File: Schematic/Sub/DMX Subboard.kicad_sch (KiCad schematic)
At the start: 6 parts, among them J1 OLED, J2 Connector, SW1 Back, SW2 Up, SW3 Down, SW4 Confirm

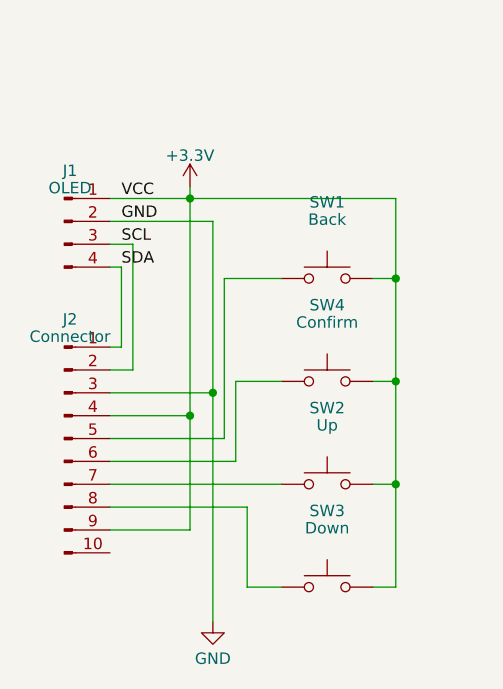
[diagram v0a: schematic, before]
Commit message: First OLED support
- SSD1306 support added
- OLED menu added (wip)
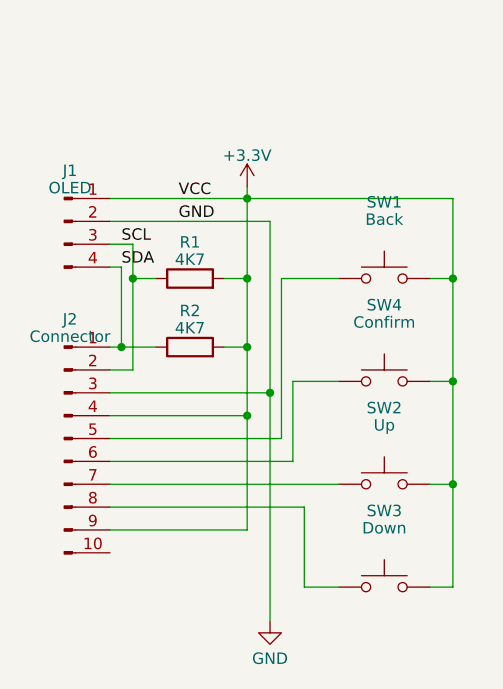
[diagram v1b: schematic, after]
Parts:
- added R1, R2: 4K7, Resistor_SMD:R_0603_1608Metric_Pad0.98x0.95mm_HandSolder, symbol Device:R
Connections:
- net +3.3V: now also R1.2, R2.2
- net SCL: now also R1.1
- net SDA: now also R2.1
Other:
- moved on the sheet: SW1, SW2, SW3, SW4

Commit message: Added support for different OLED-pinning
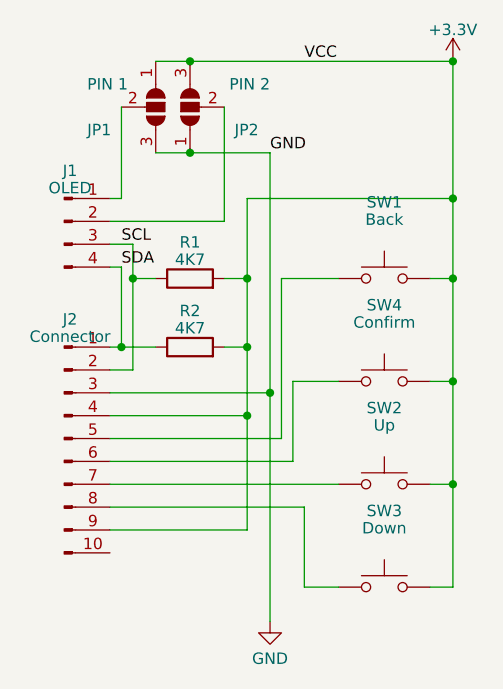
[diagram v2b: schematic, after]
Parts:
- added JP1: PIN 1, Jumper:SolderJumper-3_P2.0mm_Open_TrianglePad1.0x1.5mm, symbol Jumper:SolderJumper_3_Open
- added JP2: PIN 2, Jumper:SolderJumper-3_P2.0mm_Open_TrianglePad1.0x1.5mm, symbol Jumper:SolderJumper_3_Open
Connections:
- net +3.3V: now also JP1.1 (A), JP2.3 (B); no longer J1.1 (Pin_1)
- net GND: now also JP1.3 (B), JP2.1 (A); no longer J1.2 (Pin_2)
- new net: J1.2 (Pin_2), JP2.2 (C)
- new net: J1.1 (Pin_1), JP1.2 (C)
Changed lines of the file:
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@@
   (junction (at 69.85 54.61) (diameter 0) (color 0 0 0 0)
   )
-  (junction (at 46.99 34.29) (diameter 0) (color 0 0 0 0)
+  (junction (at 40.64 29.21) (diameter 0) (color 0 0 0 0)
+  )
+  (junction (at 40.64 19.05) (diameter 0) (color 0 0 0 0)
   )
   (junction (at 34.29 43.18) (diameter 0) (color 0 0 0 0)
@@
   (junction (at 69.85 66.04) (diameter 0) (color 0 0 0 0)
   )
+  (junction (at 69.85 19.05) (diameter 0) (color 0 0 0 0)
+  )
   (junction (at 46.99 43.18) (diameter 0) (color 0 0 0 0)
   )
+  (junction (at 69.85 34.29) (diameter 0) (color 0 0 0 0)
+  )
   (wire (pts (xy 31.75 63.5) (xy 52.07 63.5))
     (stroke (width 0) (type default))
   )
-  (wire (pts (xy 31.75 36.83) (xy 49.53 36.83))
-    (stroke (width 0) (type default))
-  )
-  (wire (pts (xy 49.53 36.83) (xy 49.53 55.88))
+  (wire (pts (xy 44.45 24.13) (xy 44.45 36.83))
+    (stroke (width 0) (type default))
+  )
+  (wire (pts (xy 49.53 29.21) (xy 49.53 55.88))
     (stroke (width 0) (type default))
   )
@@
     (stroke (width 0) (type default))
   )
-  (wire (pts (xy 31.75 34.29) (xy 46.99 34.29))
+  (wire (pts (xy 40.64 29.21) (xy 49.53 29.21))
+    (stroke (width 0) (type default))
+  )
+  (wire (pts (xy 44.45 36.83) (xy 31.75 36.83))
     (stroke (width 0) (type default))
   )
@@
     (stroke (width 0) (type default))
   )
+  (wire (pts (xy 33.02 34.29) (xy 31.75 34.29))
+    (stroke (width 0) (type default))
+  )
+  (wire (pts (xy 46.99 34.29) (xy 69.85 34.29))
+    (stroke (width 0) (type default))
+  )
   (wire (pts (xy 31.75 68.58) (xy 53.34 68.58))
     (stroke (width 0) (type default))
@@
     (stroke (width 0) (type default))
   )
-  (wire (pts (xy 46.99 33.02) (xy 46.99 34.29))
-    (stroke (width 0) (type default))
-  )
   (wire (pts (xy 34.29 53.34) (xy 34.29 43.18))
     (stroke (width 0) (type default))
@@
     (stroke (width 0) (type default))
   )
+  (wire (pts (xy 69.85 19.05) (xy 69.85 34.29))
+    (stroke (width 0) (type default))
+  )
   (wire (pts (xy 69.85 54.61) (xy 69.85 66.04))
     (stroke (width 0) (type default))
   )
-  (wire (pts (xy 69.85 34.29) (xy 46.99 34.29))
+  (wire (pts (xy 33.02 24.13) (xy 33.02 34.29))
     (stroke (width 0) (type default))
   )
@@
   )
   (wire (pts (xy 33.02 50.8) (xy 36.83 50.8))
+    (stroke (width 0) (type default))
+  )
+  (wire (pts (xy 36.83 29.21) (xy 40.64 29.21))
+    (stroke (width 0) (type default))
+  )
+  (wire (pts (xy 40.64 19.05) (xy 69.85 19.05))
+    (stroke (width 0) (type default))
+  )
+  (wire (pts (xy 36.83 19.05) (xy 40.64 19.05))
     (stroke (width 0) (type default))
   )
@@
     (effects (font (size 1.27 1.27)) (justify left bottom))
   )
-  (label "GND" (at 39.37 36.83 0) (fields_autoplaced)
+  (label "GND" (at 49.53 29.21 0) (fields_autoplaced)
     (effects (font (size 1.27 1.27)) (justify left bottom))
   )
@@
     (effects (font (size 1.27 1.27)) (justify left bottom))
   )
-  (label "VCC" (at 39.37 34.29 0) (fields_autoplaced)
+  (label "VCC" (at 53.34 19.05 0) (fields_autoplaced)
     (effects (font (size 1.27 1.27)) (justify left bottom))
   )
@@
     )
   )
+  (symbol (lib_id "Jumper:SolderJumper_3_Open") (at 40.64 24.13 90) (unit 1)
+    (in_bom yes) (on_board yes) (dnp no)
+    (property "Reference" "JP2" (at 48.26 26.67 90)
+      (effects (font (size 1.27 1.27)) (justify left))
+    )
+    (property "Value" "PIN 2" (at 49.53 21.59 90)
+      (effects (font (size 1.27 1.27)) (justify left))
+    )
+    (property "Footprint" "Jumper:SolderJumper-3_P2.0mm_Open_TrianglePad1.0x1.5mm" (at 40.64 24.13 0)
+      (effects (font (size 1.27 1.27)) hide)
+    )
+    (property "Datasheet" "~" (at 40.64 24.13 0)
+      (effects (font (size 1.27 1.27)) hide)
+    )
+    (pin "1")
+    (pin "2")
+    (pin "3")
+    (instances
+      (project "DMX Subboard"
+        (path "/9f67bc81-d3bc-45a8-a896-4f7d3309896c"
+          (reference "JP2") (unit 1)
+        )
+      )
+    )
+  )
   (symbol (lib_id "power:GND") (at 49.53 81.28 0) (unit 1)
     (in_bom yes) (on_board yes) (dnp no) (fields_autoplaced)
@@
     )
   )
-  (symbol (lib_id "power:+3.3V") (at 46.99 33.02 0) (unit 1)
-    (in_bom yes) (on_board yes) (dnp no) (fields_autoplaced)
-    (property "Reference" "#PWR01" (at 46.99 36.83 0)
-      (effects (font (size 1.27 1.27)) hide)
-    )
-    (property "Value" "+3.3V" (at 46.99 29.5181 0)
-      (effects (font (size 1.27 1.27)))
-    )
-    (property "Footprint" "" (at 46.99 33.02 0)
-      (effects (font (size 1.27 1.27)) hide)
-    )
-    (property "Datasheet" "" (at 46.99 33.02 0)
+  (symbol (lib_id "power:+3.3V") (at 69.85 19.05 0) (unit 1)
+    (in_bom yes) (on_board yes) (dnp no) (fields_autoplaced)
+    (property "Reference" "#PWR01" (at 69.85 22.86 0)
+      (effects (font (size 1.27 1.27)) hide)
+    )
+    (property "Value" "+3.3V" (at 69.85 15.5481 0)
+      (effects (font (size 1.27 1.27)))
+    )
+    (property "Footprint" "" (at 69.85 19.05 0)
+      (effects (font (size 1.27 1.27)) hide)
+    )
+    (property "Datasheet" "" (at 69.85 19.05 0)
       (effects (font (size 1.27 1.27)) hide)
     )
@@
         )
       )
+    )
+  )
+  (symbol (lib_id "Jumper:SolderJumper_3_Open") (at 36.83 24.13 270) (unit 1)
+    (in_bom yes) (on_board yes) (dnp no)
+    (property "Reference" "JP1" (at 29.21 26.67 90)
+      (effects (font (size 1.27 1.27)) (justify left))
+    )
+    (property "Value" "PIN 1" (at 29.21 21.59 90)
+      (effects (font (size 1.27 1.27)) (justify left))
+    )
+    (property "Footprint" "Jumper:SolderJumper-3_P2.0mm_Open_TrianglePad1.0x1.5mm" (at 36.83 24.13 0)
+      (effects (font (size 1.27 1.27)) hide)
+    )
+    (property "Datasheet" "~" (at 36.83 24.13 0)
+      (effects (font (size 1.27 1.27)) hide)
+    )
+    (pin "1")
+    (pin "2")
+    (pin "3")
+    (instances
+      (project "DMX Subboard"
+        (path "/9f67bc81-d3bc-45a8-a896-4f7d3309896c"
+          (reference "JP1") (unit 1)
+        )
+      )
